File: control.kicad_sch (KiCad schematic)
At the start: 41 parts, among them J4 Conn_01x05_Pin, J5 Conn_01x03_Pin, J6 Conn_01x03_Pin, Q2 AO3400, Q3 DTC143Z, Q4 DMG1012T, SW1 SW_SPDT_SH, SW2 SW_Push, U6 STM32G031G8Ux

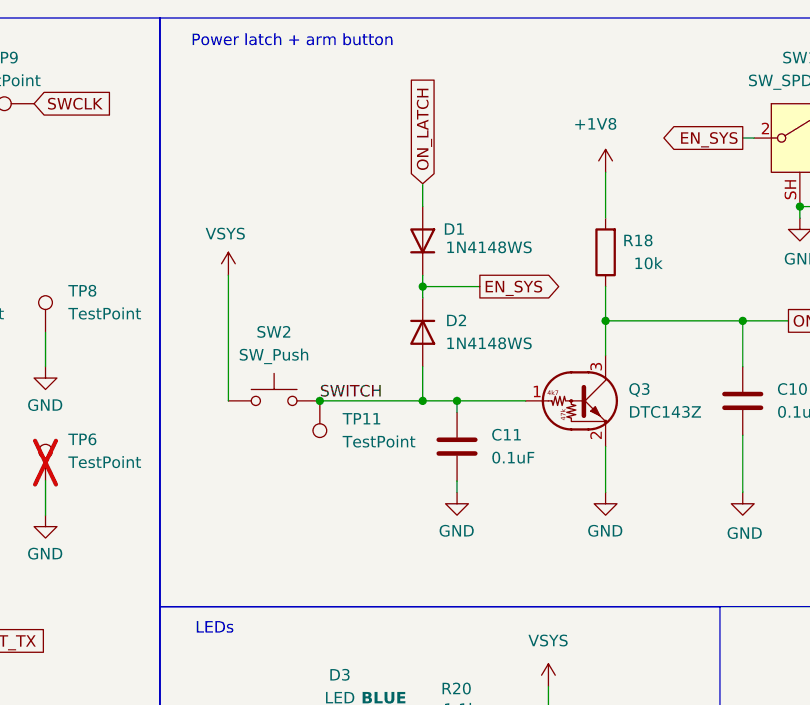
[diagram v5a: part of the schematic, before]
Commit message: v4.2 Revision - Rerouting again - New SW2
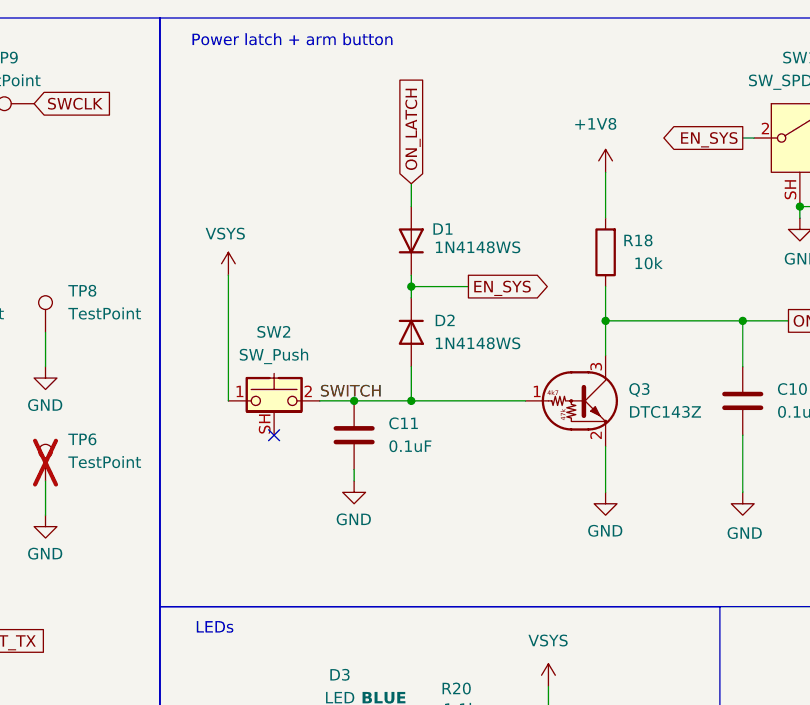
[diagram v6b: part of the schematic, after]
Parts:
- removed TP11: TestPoint, TestPoint:TestPoint_Pad_D1.0mm, symbol Connector:TestPoint
- SW1: LCSC (none) -> C109335
- SW2: footprint Button_Switch_SMD:SW_SPST_EVQP7C -> Muffin_SMD:SW_Push_1P1T-MP_NO_Horizontal_Alps_SKRTLAE010; symbol Switch:SW_Push -> Switch:SW_Push_Shielded
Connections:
- no-connect marks 10 -> 11
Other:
- moved on the sheet: C11, D1, D2

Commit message: v4.3 - Smaller, faster, stronger (lol) - Removed few appendixes - Updated doc jobs set
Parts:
- removed D2: 1N4148WS, Diode_SMD:D_SOD-323, symbol Diode:1N4148WS
- removed Q2: AO3400, Package_TO_SOT_SMD:SOT-23, symbol Transistor_FET:AO3400A
- removed R13: 10k, Resistor_SMD:R_0603_1608Metric, symbol Device:R
- removed R8: 100k, Resistor_SMD:R_0603_1608Metric, symbol Device:R
- removed TP6: TestPoint, TestPoint:TestPoint_Plated_Hole_D4.0mm, symbol Connector:TestPoint
- added Q1: AO3400A, Package_TO_SOT_SMD:SOT-23, symbol Transistor_FET:AO3400A
- R1: value 100k -> 10k
- R20, R21, R23: value 1.1k -> 3.3k
- TP1: value TestPoint -> U_TX
- TP2: value TestPoint -> U_RX
- TP4: value TestPoint -> SWDIO
- TP5: value TestPoint -> ~{NRST}
- TP7, TP8: value TestPoint -> GND
- TP9: value TestPoint -> SWCLK
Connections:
- net +BATT: now also Q1.3 (D)
- net EN_LOAD_BATT: now also R1.1
- net GND: no longer R1.2
- net at Q4.1 (G), R22.2: no longer R1.1
- net at R16.2: now also Q1.2 (S)
- new net: Q1.1 (G), R1.2
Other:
- moved on the sheet: C9, D1, R16, R17, R22
